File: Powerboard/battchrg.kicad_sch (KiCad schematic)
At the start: 60 parts, among them IC1 BQ24618RGET-iclr, J1 Thermistor Connection 103AT N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, J5 Conn_01x04_Male, J6 Conn_01x02_Male, J7 IsolationSwitch, Q1 RSJ250P10TL, Q2 RSJ250P10TL, Q3 RSJ250P10TL, Q4 RS1G120MN, Q5 RS1G120MN

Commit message: All capacitors selected, most other footprints assigned
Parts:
- C12, C13, C16, C8, C9: footprint (none) -> Capacitor_SMD:C_0805_2012Metric
- C5, C7, CTTC1: footprint (none) -> Capacitor_SMD:C_0603_1608Metric
- IC1: footprint (none) -> Package_DFN_QFN:VQFN-24-1EP_4x4mm_P0.5mm_EP2.45x2.45mm
- Q1, Q2, Q3: footprint (none) -> Package_TO_SOT_SMD:TO-263-3_TabPin2
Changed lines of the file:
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@@
       (effects (font (size 1.27 1.27)) (justify left))
     )
-    (property "Footprint" "" (id 2) (at 241.3 87.63 0)
+    (property "Footprint" "Package_DFN_QFN:VQFN-24-1EP_4x4mm_P0.5mm_EP2.45x2.45mm" (id 2) (at 241.3 87.63 0)
       (effects (font (size 1.27 1.27)) (justify left) hide)
     )
@@
       (effects (font (size 1.27 1.27)) (justify left))
     )
-    (property "Footprint" "" (id 2) (at 87.63 60.96 0)
+    (property "Footprint" "Package_TO_SOT_SMD:TO-263-3_TabPin2" (id 2) (at 87.63 60.96 0)
       (effects (font (size 1.27 1.27)) (justify left) hide)
     )
@@
       (effects (font (size 1.27 1.27)) (justify left))
     )
-    (property "Footprint" "" (id 2) (at 215.9 45.72 0)
+    (property "Footprint" "Package_TO_SOT_SMD:TO-263-3_TabPin2" (id 2) (at 215.9 45.72 0)
       (effects (font (size 1.27 1.27)) (justify left) hide)
     )
@@
       (effects (font (size 1.27 1.27)) (justify left))
     )
-    (property "Footprint" "" (id 2) (at 123.19 107.95 0)
+    (property "Footprint" "Capacitor_SMD:C_0603_1608Metric" (id 2) (at 123.19 107.95 0)
       (effects (font (size 1.27 1.27)) hide)
     )
@@
       (effects (font (size 1.27 1.27)) (justify left))
     )
-    (property "Footprint" "" (id 2) (at 168.91 81.28 0)
+    (property "Footprint" "Capacitor_SMD:C_0805_2012Metric" (id 2) (at 168.91 81.28 0)
       (effects (font (size 1.27 1.27)) hide)
     )
@@
       (effects (font (size 1.27 1.27)) (justify left))
     )
-    (property "Footprint" "" (id 2) (at 80.01 129.54 0)
+    (property "Footprint" "Capacitor_SMD:C_0805_2012Metric" (id 2) (at 80.01 129.54 0)
       (effects (font (size 1.27 1.27)) hide)
     )
@@
       (effects (font (size 1.27 1.27)) (justify left))
     )
-    (property "Footprint" "" (id 2) (at 219.71 137.16 0)
+    (property "Footprint" "Capacitor_SMD:C_0603_1608Metric" (id 2) (at 219.71 137.16 0)
       (effects (font (size 1.27 1.27)) hide)
     )
@@
       (effects (font (size 1.27 1.27)) (justify left))
     )
-    (property "Footprint" "" (id 2) (at 73.66 129.54 0)
+    (property "Footprint" "Capacitor_SMD:C_0805_2012Metric" (id 2) (at 73.66 129.54 0)
       (effects (font (size 1.27 1.27)) hide)
     )
@@
       (effects (font (size 1.27 1.27)) (justify left))
     )
-    (property "Footprint" "" (id 2) (at 173.99 90.17 0)
+    (property "Footprint" "Package_TO_SOT_SMD:TO-263-3_TabPin2" (id 2) (at 173.99 90.17 0)
       (effects (font (size 1.27 1.27)) (justify left) hide)
     )
@@
       (effects (font (size 1.27 1.27)) (justify left))
     )
-    (property "Footprint" "" (id 2) (at 73.66 64.77 0)
+    (property "Footprint" "Capacitor_SMD:C_0805_2012Metric" (id 2) (at 73.66 64.77 0)
       (effects (font (size 1.27 1.27)) hide)
     )
@@
       (effects (font (size 1.27 1.27)) (justify left))
     )
-    (property "Footprint" "" (id 2) (at 251.46 102.87 0)
+    (property "Footprint" "Capacitor_SMD:C_0603_1608Metric" (id 2) (at 251.46 102.87 0)
       (effects (font (size 1.27 1.27)) hide)
     )
@@
       (effects (font (size 1.27 1.27)) (justify left))
     )
-    (property "Footprint" "" (id 2) (at 179.07 81.28 0)
-      (effects (font (size 1.27 1.27)) hide)
-    )
+    (property "Footprint" "Capacitor_SMD:C_0805_2012Metric" (id 2) (at 179.07 81.28 0)
+      (effects (font (size 1.27 1.27)) hide)
+    )

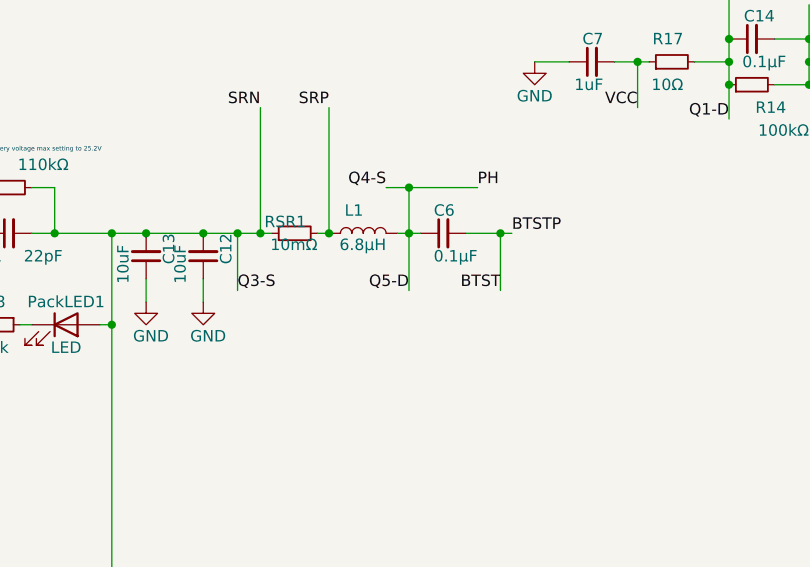
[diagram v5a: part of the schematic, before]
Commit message: Finished footprint assignment
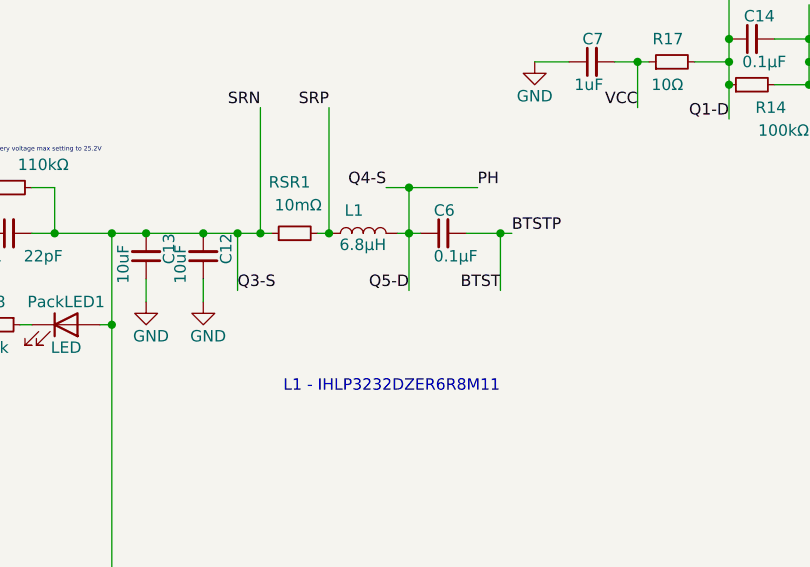
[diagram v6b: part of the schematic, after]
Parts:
- J1: footprint (none) -> Connector_JST:JST_XH_B2B-XH-AM_1x02_P2.50mm_Vertical
- L1: footprint (none) -> iclr:INDM8681X400N
- R20, R28, R29, R30, R31, R32, RAC1, RAdp1, RFast1, RPre1, RSR1: footprint (none) -> Resistor_SMD:R_0603_1608Metric
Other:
- note added: "L1 - IHLP3232DZER6R8M11"
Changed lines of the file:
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@@
     (effects (font (size 0.5 0.5)) (justify left bottom))
+  )
+  (text "L1 - IHLP3232DZER6R8M11 " (at 88.9 144.78 0)
+    (effects (font (size 1.27 1.27)) (justify left bottom))
   )
   (text "R8: Fast Charging Current to 4A" (at 255.27 157.48 0)
@@
     (property "Reference" "RAC1" (id 0) (at 203.2 91.5416 90))
     (property "Value" "10mΩ" (id 1) (at 203.2 93.853 90))
-    (property "Footprint" "" (id 2) (at 203.2 96.52 0)
+    (property "Footprint" "Resistor_SMD:R_0603_1608Metric" (id 2) (at 203.2 96.52 0)
       (effects (font (size 1.27 1.27)) hide)
     )
@@
     (property "Reference" "J1" (id 0) (at 170.18 118.11 0))
     (property "Value" "Thermistor Connection 103AT NTC" (id 1) (at 163.83 120.65 0))
-    (property "Footprint" "" (id 2) (at 172.72 118.11 0)
+    (property "Footprint" "Connector_JST:JST_XH_B2B-XH-AM_1x02_P2.50mm_Vertical" (id 2) (at 172.72 118.11 0)
       (effects (font (size 1.27 1.27)) hide)
     )
@@
       (effects (font (size 1.27 1.27)) (justify left))
     )
-    (property "Footprint" "" (id 2) (at 239.522 151.13 90)
+    (property "Footprint" "Resistor_SMD:R_0603_1608Metric" (id 2) (at 239.522 151.13 90)
       (effects (font (size 1.27 1.27)) hide)
     )
@@
       (effects (font (size 1.27 1.27)) (justify left))
     )
-    (property "Footprint" "" (id 2) (at 252.222 151.13 90)
+    (property "Footprint" "Resistor_SMD:R_0603_1608Metric" (id 2) (at 252.222 151.13 90)
       (effects (font (size 1.27 1.27)) hide)
     )
@@
       (effects (font (size 1.27 1.27)) (justify left))
     )
-    (property "Footprint" "" (id 2) (at 245.872 151.13 90)
+    (property "Footprint" "Resistor_SMD:R_0603_1608Metric" (id 2) (at 245.872 151.13 90)
       (effects (font (size 1.27 1.27)) hide)
     )
@@
       (effects (font (size 1.27 1.27)) (justify left))
     )
-    (property "Footprint" "" (id 2) (at 73.66 59.69 0)
+    (property "Footprint" "Resistor_SMD:R_0603_1608Metric" (id 2) (at 73.66 59.69 0)
       (effects (font (size 1.27 1.27)) hide)
     )
@@
       (effects (font (size 1.27 1.27)) (justify left))
     )
-    (property "Footprint" "" (id 2) (at 215.9 72.39 0)
+    (property "Footprint" "Resistor_SMD:R_0603_1608Metric" (id 2) (at 215.9 72.39 0)
       (effects (font (size 1.27 1.27)) hide)
     )
@@
   (symbol (lib_id "Device:R_Small") (at 90.17 127 90) (unit 1)
     (in_bom yes) (on_board yes)
-    (property "Reference" "RSR1" (id 0) (at 91.44 125.73 90)
-      (effects (font (size 1.27 1.27)) (justify left))
-    )
-    (property "Value" "10mΩ" (id 1) (at 92.71 128.27 90)
-      (effects (font (size 1.27 1.27)) (justify left))
-    )
-    (property "Footprint" "" (id 2) (at 90.17 127 0)
+    (property "Reference" "RSR1" (id 0) (at 91.9084 121.326 90)
+      (effects (font (size 1.27 1.27)) (justify left))
+    )
+    (property "Value" "10mΩ" (id 1) (at 93.1784 123.866 90)
+      (effects (font (size 1.27 1.27)) (justify left))
+    )
+    (property "Footprint" "Resistor_SMD:R_0603_1608Metric" (id 2) (at 90.17 127 0)
       (effects (font (size 1.27 1.27)) hide)
     )
@@
       (effects (font (size 1.27 1.27)) (justify left))
     )
-    (property "Footprint" "" (id 2) (at 97.79 127 0)
+    (property "Footprint" "iclr:INDM8681X400N" (id 2) (at 97.79 127 0)
       (effects (font (size 1.27 1.27)) hide)
     )
@@
       (effects (font (size 1.27 1.27)) (justify left))
     )
-    (property "Footprint" "" (id 2) (at 67.31 46.99 0)
+    (property "Footprint" "Resistor_SMD:R_0603_1608Metric" (id 2) (at 67.31 46.99 0)
       (effects (font (size 1.27 1.27)) hide)
     )
@@
       (effects (font (size 1.27 1.27)) (justify left))
     )
-    (property "Footprint" "" (id 2) (at 57.15 137.16 0)
+    (property "Footprint" "Resistor_SMD:R_0603_1608Metric" (id 2) (at 57.15 137.16 0)
       (effects (font (size 1.27 1.27)) hide)
     )
@@
     (property "Reference" "R30" (id 0) (at 99.314 176.4116 90))
     (property "Value" "75k" (id 1) (at 99.314 178.9485 90))
-    (property "Footprint" "" (id 2) (at 99.314 180.848 0)
+    (property "Footprint" "Resistor_SMD:R_0603_1608Metric" (id 2) (at 99.314 180.848 0)
       (effects (font (size 1.27 1.27)) hide)
     )
@@
     (property "Reference" "R31" (id 0) (at 109.474 176.4116 90))
     (property "Value" "10k" (id 1) (at 109.474 178.9485 90))
-    (property "Footprint" "" (id 2) (at 109.474 180.848 0)
-      (effects (font (size 1.27 1.27)) hide)
-    )
+    (property "Footprint" "Resistor_SMD:R_0603_1608Metric" (id 2) (at 109.474 180.848 0)
+      (effects (font (size 1.27 1.27)) hide)
+    )

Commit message: changed some FP assignments and imported components
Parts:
- J5: footprint Connector_Molex:Molex_Mini-Fit_Jr_5566-08A2_2x04_P4.20mm_Vertical -> Connector_Molex:Molex_Mini-Fit_Jr_5566-04A_2x02_P4.20mm_Vertical
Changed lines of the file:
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@@
     (property "Reference" "J5" (id 0) (at 22.86 50.8 0))
     (property "Value" "Conn_01x04_Male" (id 1) (at 15.367 45.085 0))
-    (property "Footprint" "Connector_Molex:Molex_Mini-Fit_Jr_5566-08A2_2x04_P4.20mm_Vertical" (id 2) (at 18.923 57.023 0)
+    (property "Footprint" "Connector_Molex:Molex_Mini-Fit_Jr_5566-04A_2x02_P4.20mm_Vertical" (id 2) (at 18.923 57.023 0)
       (effects (font (size 1.27 1.27)) hide)
     )

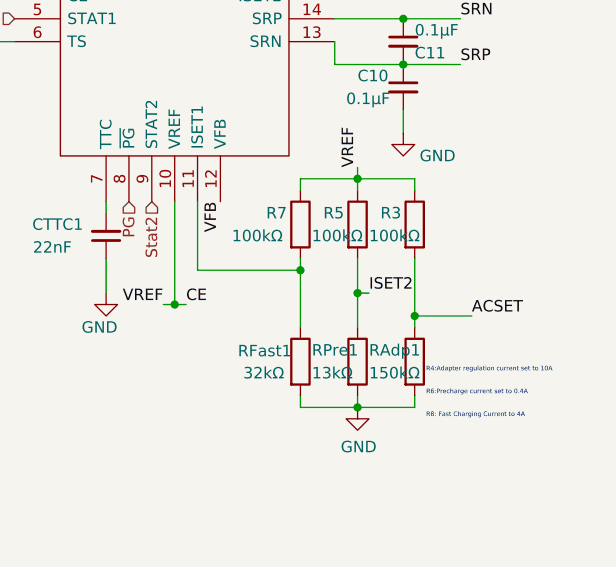
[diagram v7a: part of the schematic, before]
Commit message: moving around charger components
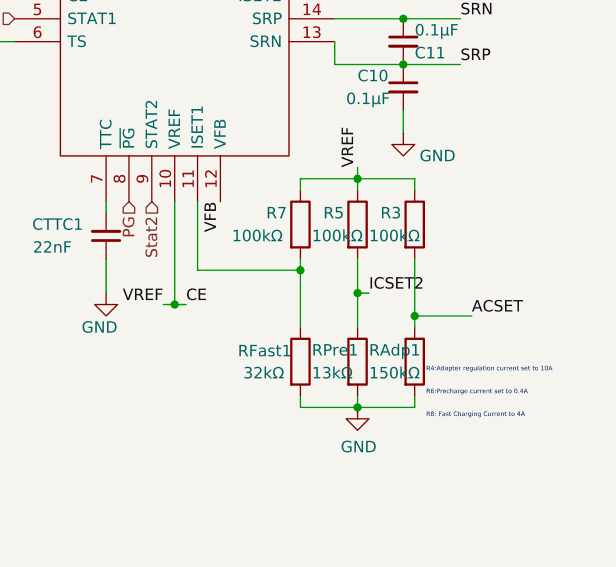
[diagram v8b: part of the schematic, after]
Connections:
- net ISET2 is gone; now on net ICSET2: R5.2, RPre1.1
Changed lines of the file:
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@@
     (effects (font (size 1.27 1.27)) (justify left bottom))
   )
-  (label "ISET2" (at 248.92 143.51 0)
+  (label "ICSET2" (at 248.92 143.51 0)
     (effects (font (size 1.27 1.27)) (justify left bottom))
   )
